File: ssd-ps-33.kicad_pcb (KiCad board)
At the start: 2 copper layers, 0 parts

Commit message: Preliminary place components
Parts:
- added C1: 10uF, Capacitor_SMD:C_0805_2012Metric, F.Cu at (143.4, 96.6)
- added C2: 10uF, Capacitor_SMD:C_0805_2012Metric, F.Cu at (140.7, 95.7)
- added C3: 0.1uF, Capacitor_SMD:C_0603_1608Metric_Pad1.08x0.95mm_HandSolder, F.Cu at (143.4, 98.3)
- added C4: 22uF, Capacitor_SMD:C_0805_2012Metric, F.Cu at (144.5, 102.7)
- added C5: 22uF, Capacitor_SMD:C_0805_2012Metric, F.Cu at (146.5, 102.7)
- added C6: 22uF, Capacitor_SMD:C_0805_2012Metric, F.Cu at (147.4, 105.4)
- added C7: 0.1uF, Capacitor_SMD:C_0603_1608Metric_Pad1.08x0.95mm_HandSolder, F.Cu at (150.0, 99.1)
- added C8: 0.1uF, Capacitor_SMD:C_0603_1608Metric_Pad1.08x0.95mm_HandSolder, F.Cu at (150.0, 104.0)
- added D1: 5.6V, Diode_SMD:D_SOD-323_HandSoldering, F.Cu at (154.7, 104.4)
- added L1: 2.2µH, Inductor_SMD:L_Chilisin_BWVS00505040, F.Cu at (140.7, 102.5)
- added R1: R, Resistor_SMD:R_0603_1608Metric_Pad0.98x0.95mm_HandSolder, F.Cu at (153.0, 104.0)
- added R2: R, Resistor_SMD:R_0603_1608Metric_Pad0.98x0.95mm_HandSolder, F.Cu at (151.5, 104.0)
- added R3: 51, Resistor_SMD:R_0603_1608Metric_Pad0.98x0.95mm_HandSolder, F.Cu at (152.4, 98.2)
- added R4: 135k, Resistor_SMD:R_0603_1608Metric_Pad0.98x0.95mm_HandSolder, F.Cu at (150.0, 97.3)
- added R5: 30k, Resistor_SMD:R_0603_1608Metric_Pad0.98x0.95mm_HandSolder, F.Cu at (147.6, 98.2)
- added R6: 10k, Resistor_SMD:R_0603_1608Metric_Pad0.98x0.95mm_HandSolder, F.Cu at (151.2, 95.3)
- added U1: TPS563252, Package_TO_SOT_SMD:SOT-563, F.Cu at (144.7, 100.0)

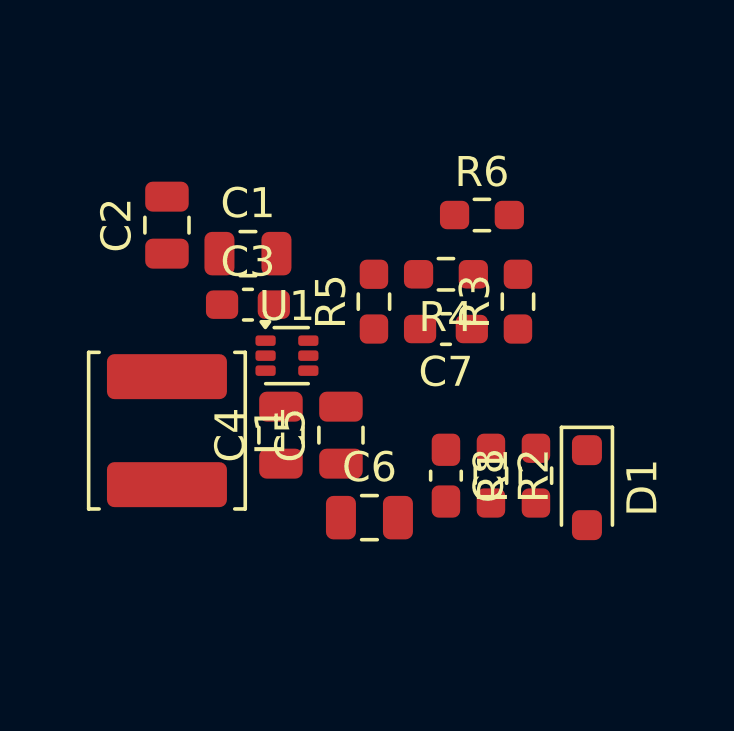
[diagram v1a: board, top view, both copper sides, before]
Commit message: Draft routing, board size and select connectors
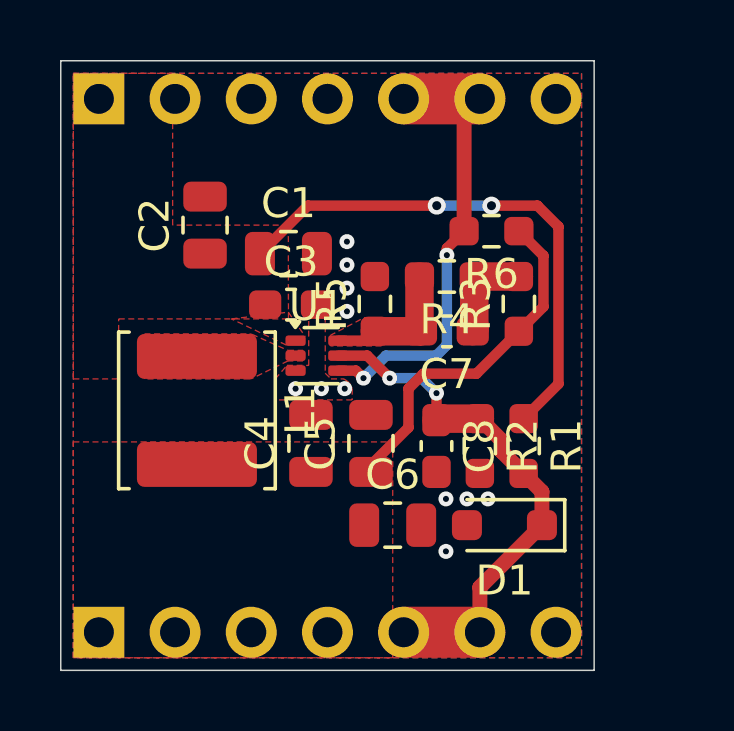
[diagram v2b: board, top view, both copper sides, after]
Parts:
- added J1: Top, ssd-ps-33:PinHeader_1x07_P2.54mm_Vertical_No_Silkscreen, B.Cu at (138.4, 91.4)
- added J2: Bottom, ssd-ps-33:PinHeader_1x07_P2.54mm_Vertical_No_Silkscreen, B.Cu at (138.4, 109.2)
- moved D1 3.02 mm to (151.9, 105.7), turned to 180 degrees
- moved C3 1.44 mm to (144.8, 98.3)
- moved C1 1.35 mm to (144.8, 96.6)
- moved C2 1.27 mm to (142.0, 95.7)
- moved L1 1.21 mm to (141.7, 101.8)
- moved R1 1.07 mm to (152.6, 103.0), turned to -90 degrees
- moved R2 1.05 mm to (151.1, 103.0)
- moved C4 1.04 mm to (145.5, 102.9)
- moved C5 1.04 mm to (147.5, 102.9)
- moved C8 1.04 mm to (149.7, 103.0)
- moved U1 1.00 mm to (145.7, 100.0)
- moved C6 0.81 mm to (148.2, 105.7)
- moved R6 0.62 mm to (151.5, 95.8), turned to 180 degrees
- moved C7 0.08 mm to (150.0, 99.2)
- moved R3 0.08 mm to (152.4, 98.3)
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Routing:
- net /VIN: track 0.00 -> 17.9 mm, vias 0 -> 2
- net /EN: track 0.00 -> 17.5 mm, vias 0 -> 2
- net /PG: track 0.00 -> 15.4 mm, vias 0 -> 2
- net /VOUT: track 0.00 -> 11.8 mm
- net /FB: track 0.00 -> 4.73 mm
- net Net-(C7-Pad1): track 0.00 -> 3.33 mm
- net GND: vias 0 -> 11
- added copper zone on F.Cu, net /FB
- added copper zone on F.Cu, net /VIN
- added copper zone on F.Cu, net /VOUT
- added copper zone on B.Cu, net GND
- added copper zone on F.Cu, net GND
- added copper zone on F.Cu, net Net-(U1-SW)
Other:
- board outline added: 17.8 x 20.3 mm

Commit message: Set values for enable network and fix DRC errors
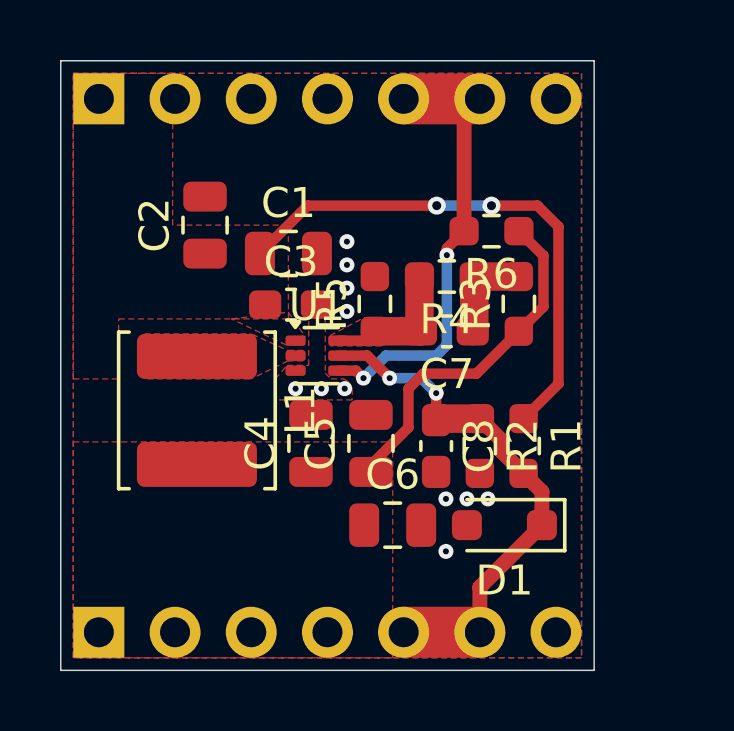
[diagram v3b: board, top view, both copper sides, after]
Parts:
- R1: value R -> 51k
- R2: value R -> 27k
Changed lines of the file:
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@@
 			)
 		)
-		(property "Value" "R"
+		(property "Value" "27k"
 			(at 0 1.43 90)
 			(layer "F.Fab")
@@
 			)
 		)
-		(property "Description" "5%, 0.1 W, AEC-Q200 Grade 0"
+		(property "Description" "1%, 0.1 W"
 			(at 0 0 90)
 			(layer "F.Fab")
@@
 			)
 		)
-		(property "Value" "R"
+		(property "Value" "51k"
 			(at 0 1.43 90)
 			(layer "F.Fab")
@@
 			)
 		)
-		(property "Description" "5%, 0.1 W, AEC-Q200 Grade 0"
+		(property "Description" "1%, 0.1 W"
 			(at 0 0 90)
 			(layer "F.Fab")
@@
 	(footprint "Capacitor_SMD:C_0805_2012Metric"
 		(layer "F.Cu")
-		(at 144.75 96.6)
+		(at 144.75 96.595)
 		(descr "Capacitor SMD 0805 (2012 Metric), square (rectangular) end terminal, IPC-7351 nominal, (Body size source: IPC-SM-782 page 76, https://www.pcb-3d.com/wordpress/wp-content/uploads/ipc-sm-782a_amendment_1_and_2.pdf, https://docs.google.com/spreadsheets/d/1BsfQQcO9C6DZCsRaXUlFlo91Tg2WpOkGARC1WS5S8t0/edit?usp=sharing), generated with kicad-footprint-generator")
 		(tags "capacitor")
@@
 	(footprint "Capacitor_SMD:C_0603_1608Metric_Pad1.08x0.95mm_HandSolder"
 		(layer "F.Cu")
-		(at 149.685 103.0125 -90)
+		(at 149.675 103.0125 -90)
 		(descr "Capacitor SMD 0603 (1608 Metric), square (rectangular) end terminal, IPC-7351 nominal with elongated pad for handsoldering. (Body size source: IPC-SM-782 page 76, https://www.pcb-3d.com/wordpress/wp-content/uploads/ipc-sm-782a_amendment_1_and_2.pdf), generated with kicad-footprint-generator")
 		(tags "capacitor handsolder")
@@
 	)
 	(segment
-		(start 149.79 95)
-		(end 145.4 95)
+		(start 153.75 95.7)
+		(end 153.05 95)
 		(width 0.35)
 		(layer "F.Cu")
@@
 	)
 	(segment
-		(start 153.75 95.7)
-		(end 153.05 95)
+		(start 149.79 95)
+		(end 145.395 95)
 		(width 0.35)
 		(layer "F.Cu")
@@
 	)
 	(segment
-		(start 145.4 95)
-		(end 143.8 96.6)
+		(start 145.395 95)
+		(end 143.8 96.595)
 		(width 0.35)
 		(layer "F.Cu")
@@
 	)
 	(segment
-		(start 149.685 101.25)
-		(end 149.685 102.15)
-		(width 0.35)
+		(start 151.13 107.72)
+		(end 151.13 109.22)
+		(width 0.5)
 		(layer "F.Cu")
 		(net 6)
 	)
 	(segment
-		(start 149.735 102.1)
-		(end 149.685 102.15)
+		(start 151.13 102.1)
+		(end 149.725 102.1)
 		(width 0.95)
 		(layer "F.Cu")
@@
 	)
 	(segment
-		(start 151.13 107.72)
-		(end 151.13 109.22)
-		(width 0.5)
-		(layer "F.Cu")
-		(net 6)
-	)
-	(segment
 		(start 151.13 109.22)
 		(end 148.59 109.22)
@@
 	)
 	(segment
-		(start 151.13 102.1)
-		(end 149.735 102.1)
+		(start 149.725 102.1)
+		(end 149.675 102.15)
 		(width 0.95)
 		(layer "F.Cu")
@@
 	)
 	(segment
+		(start 149.675 101.25)
+		(end 149.675 102.15)
+		(width 0.35)
+		(layer "F.Cu")
+		(net 6)
+	)
+	(segment
 		(start 153.2 105.65)
 		(end 153.2 104.535)
@@
 	)
 	(via
-		(at 149.685 101.25)
+		(at 149.675 101.25)
 		(size 0.5)
 		(drill 0.2)
@@
 	)
 	(segment
-		(start 148.125 100.75)
-		(end 149.185 100.75)
+		(start 149.175 100.75)
+		(end 149.675 101.25)
 		(width 0.35)
 		(layer "B.Cu")
@@
 	)
 	(segment
-		(start 149.185 100.75)
-		(end 149.685 101.25)
+		(start 148.125 100.75)
+		(end 149.175 100.75)
 		(width 0.35)
 		(layer "B.Cu")

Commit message: Place part's references
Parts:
- moved C1 2.94 mm to (142.0, 95.7), turned to 90 degrees
- moved C2 2.88 mm to (144.8, 96.4), turned to 0 degrees
- moved C3 0.20 mm to (144.8, 98.1)
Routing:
- net /PG: track 15.4 -> 15.9 mm

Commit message: Add designators to pins and board name
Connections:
- J1 pad 2: GND -> /VIN
- J2 pad 2: GND -> /VOUT
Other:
- board text added: "BATTERY - 3.3V"
- board text added: "EN"
- board text added: "G"
- board text added: "GND"
- board text added: "PG"
- board text added: "VIN"
- board text added: "VOUT"
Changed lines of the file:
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@@
 		(tags "bwvs")
 		(property "Reference" "L1"
-			(at -3.03 2.93 0)
+			(at -3.03 2.26 0)
 			(layer "F.SilkS")
 			(effects
 				(font
-					(size 1 1)
+					(size 0.8 0.8)
 					(thickness 0.16)
 				)
@@
 			(layers "*.Cu" "*.Mask")
 			(remove_unused_layers no)
-			(net 2 "GND")
+			(net 3 "/VOUT")
 			(pinfunction "Pin_2")
 			(pintype "passive")
@@
 			(layers "*.Cu" "*.Mask")
 			(remove_unused_layers no)
-			(net 2 "GND")
+			(net 1 "/VIN")
 			(pinfunction "Pin_2")
 			(pintype "passive")
@@
 		(layer "Edge.Cuts")
 	)
+	(gr_text "GND"
+		(at 144.78 107.45 0)
+		(layer "F.SilkS")
+		(effects
+			(font
+				(size 0.8 0.8)
+				(thickness 0.2)
+			)
+		)
+	)
+	(gr_text "G"
+		(at 153.67 107.45 0)
+		(layer "F.SilkS")
+		(effects
+			(font
+				(size 0.8 0.8)
+				(thickness 0.2)
+			)
+		)
+	)
+	(gr_text "GND"
+		(at 144.78 93.29 0)
+		(layer "F.SilkS")
+		(effects
+			(font
+				(size 0.8 0.8)
+				(thickness 0.2)
+			)
+		)
+	)
+	(gr_text "G"
+		(at 153.67 93.29 0)
+		(layer "F.SilkS")
+		(effects
+			(font
+				(size 0.8 0.8)
+				(thickness 0.2)
+			)
+		)
+	)
+	(gr_text "PG"
+		(at 149.86 93.29 0)
+		(layer "F.SilkS")
+		(effects
+			(font
+				(size 0.8 0.8)
+				(thickness 0.2)
+			)
+		)
+	)
+	(gr_text "VOUT"
+		(at 139.7 107.45 0)
+		(layer "F.SilkS")
+		(effects
+			(font
+				(size 0.8 0.8)
+				(thickness 0.2)
+			)
+		)
+	)
+	(gr_text "VIN"
+		(at 139.7 93.29 0)
+		(layer "F.SilkS")
+		(effects
+			(font
+				(size 0.8 0.8)
+				(thickness 0.2)
+			)
+		)
+	)
+	(gr_text "EN"
+		(at 149.86 107.45 0)
+		(layer "F.SilkS")
+		(effects
+			(font
+				(size 0.8 0.8)
+				(thickness 0.2)
+			)
+		)
+	)
+	(gr_text "BATTERY - 3.3V"
+		(at 137.63 100.33 90)
+		(layer "F.SilkS")
+		(effects
+			(font
+				(size 0.8 0.8)
+				(thickness 0.2)
+			)
+			(justify top)
+		)
+	)
 	(dimension
 		(type orthogonal)
@@
 		(polygon
 			(pts
-				(xy 139.09 100.775) (xy 139.09 98.775) (xy 144.75 98.775) (xy 144.745 95.65) (xy 140.89 95.65) (xy 140.89 90.59)
-				(xy 137.58 90.59) (xy 137.58 100.775)
+				(xy 139.09 100.775) (xy 139.09 98.775) (xy 144.75 98.775) (xy 144.745 95.65) (xy 140.89 95.65) (xy 140.895 92.5)
+				(xy 142.24 92.5) (xy 142.24 90.59) (xy 137.58 90.59) (xy 137.58 100.775)
 			)
 		)
@@
 			)
 		)
+	)
+	(zone
+		(net 0)
+		(net_name "")
+		(layer "F.Cu")
+		(hatch edge 0.5)
+		(connect_pads
+			(clearance 0)
+		)
+		(min_thickness 0.25)
+		(filled_areas_thickness no)
+		(keepout
+			(tracks allowed)
+			(vias allowed)
+			(pads allowed)
+			(copperpour not_allowed)
+			(footprints allowed)
+		)
+		(placement
+			(enabled no)
+			(sheetname "/")
+		)
+		(fill
+			(thermal_gap 0.5)
+			(thermal_bridge_width 0.5)
+		)
+		(polygon
+			(pts
+				(xy 142.8 108.8) (xy 142.8 110.07) (xy 147.6 110.07) (xy 147.6 108.8)
+			)
+		)

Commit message: Change board name and add revision
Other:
- board text added: "SSD BAT - 3.3V r.${REVISION}"
- board text removed: "BATTERY - 3.3V"
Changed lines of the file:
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@@
 		)
 	)
-	(gr_text "BATTERY - 3.3V"
-		(at 137.63 100.33 90)
+	(gr_text "SSD BAT - 3.3V r.${REVISION}"
+		(at 137.63 100.1 90)
 		(layer "F.SilkS")
 		(effects

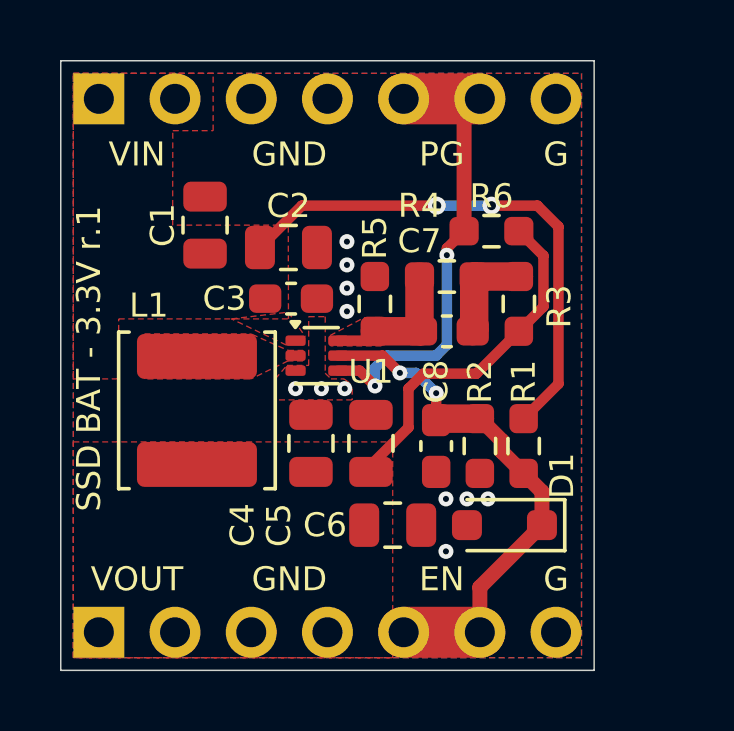
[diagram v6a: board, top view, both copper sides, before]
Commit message: Add FB to top connector and finalize routing
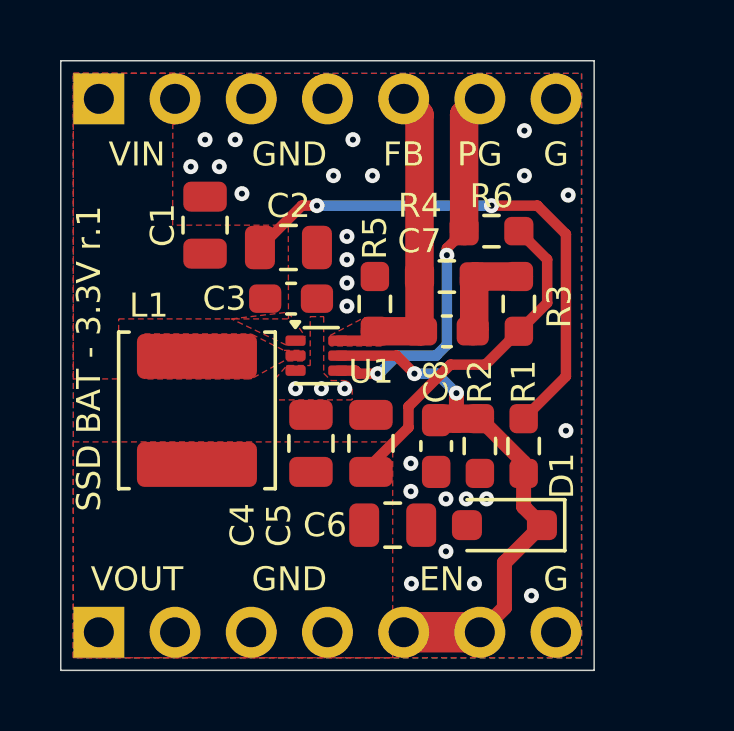
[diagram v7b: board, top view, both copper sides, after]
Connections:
- J1 pad 5: /PG -> /FB
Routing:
- net /FB: track 4.73 -> 10.9 mm
- net /PG: track 15.9 -> 12.7 mm
- net /EN: track 17.5 -> 18.2 mm
- net GND: vias 11 -> 28
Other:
- board text added: "FB"
